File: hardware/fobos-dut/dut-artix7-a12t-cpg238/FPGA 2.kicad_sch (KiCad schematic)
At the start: 7 parts, among them U7 XC7A12T-CPG238

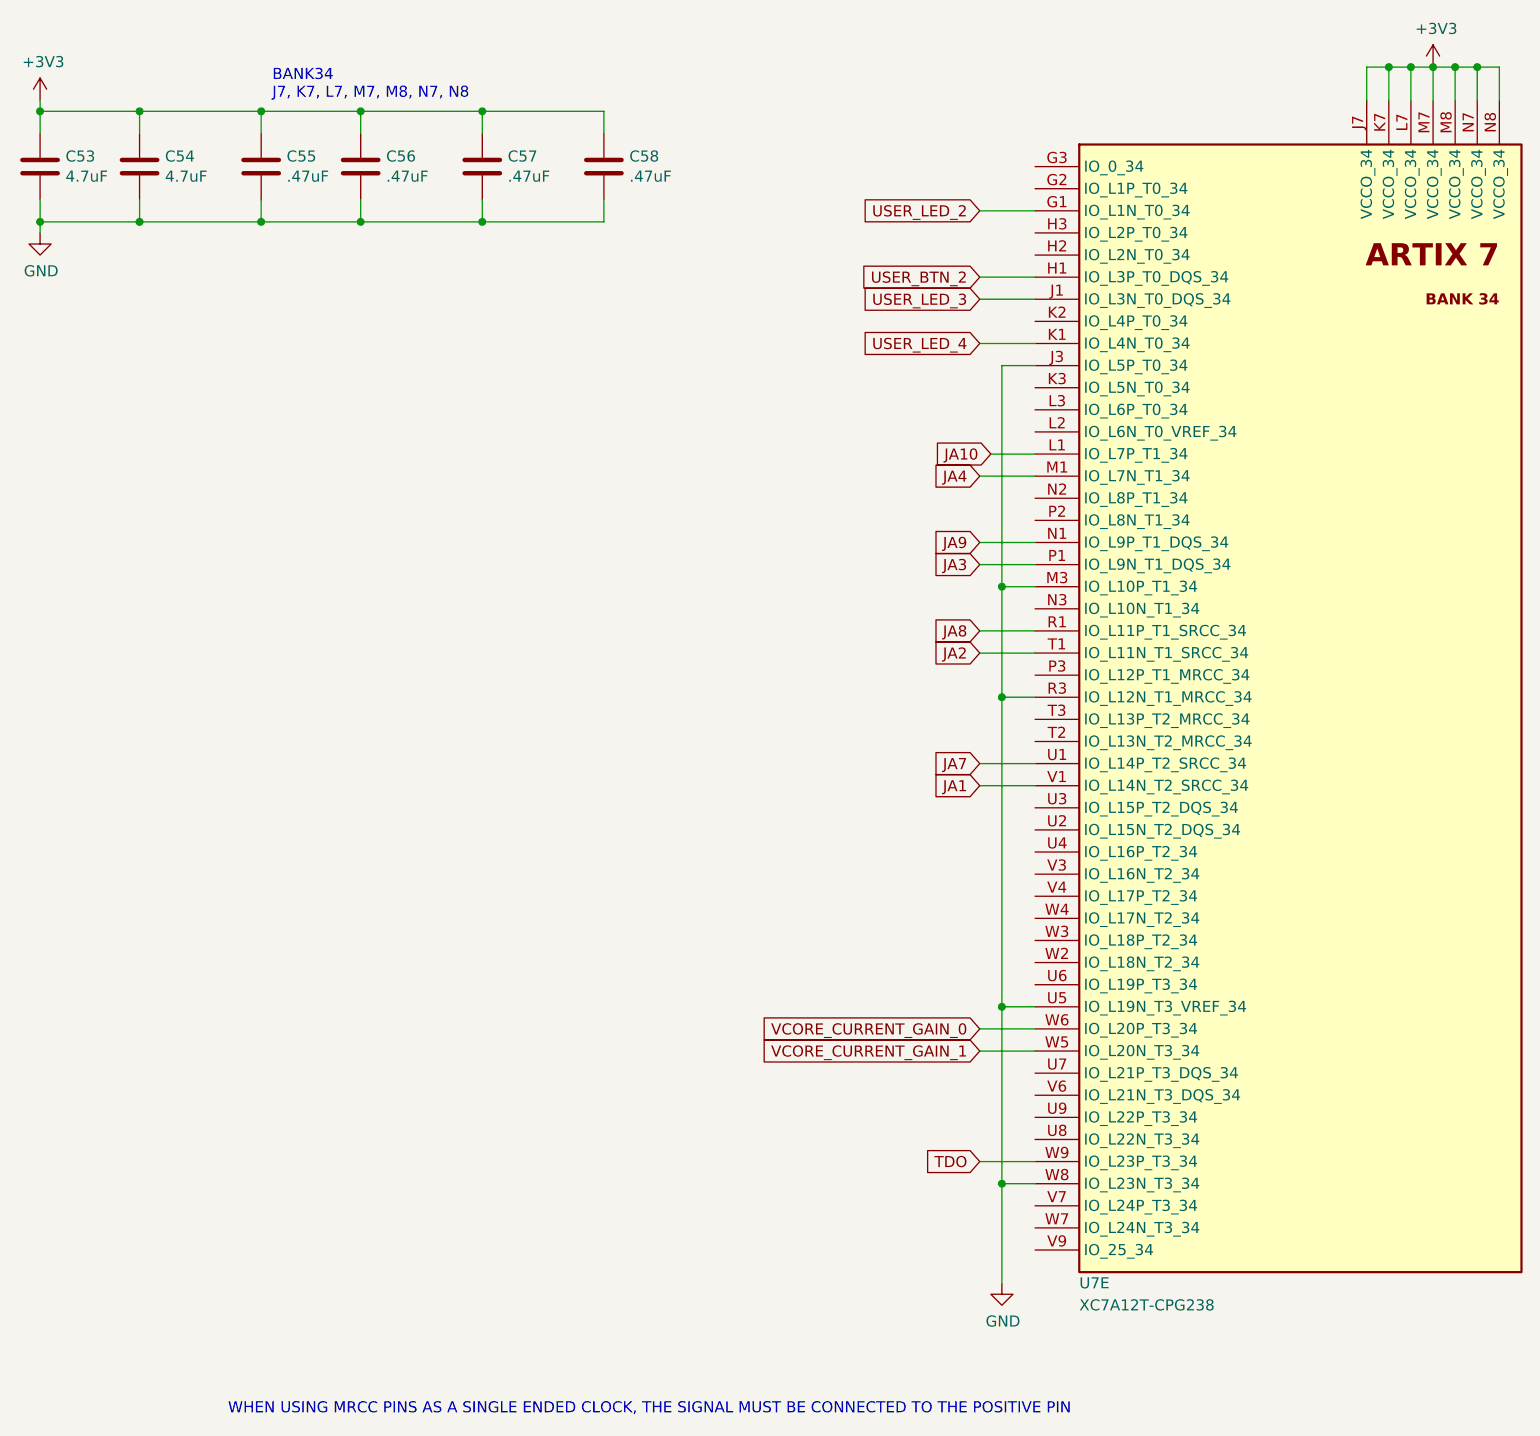
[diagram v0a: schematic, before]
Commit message: cleaned up FBDA7 rev1 added BOM, fixed bugs in schematic
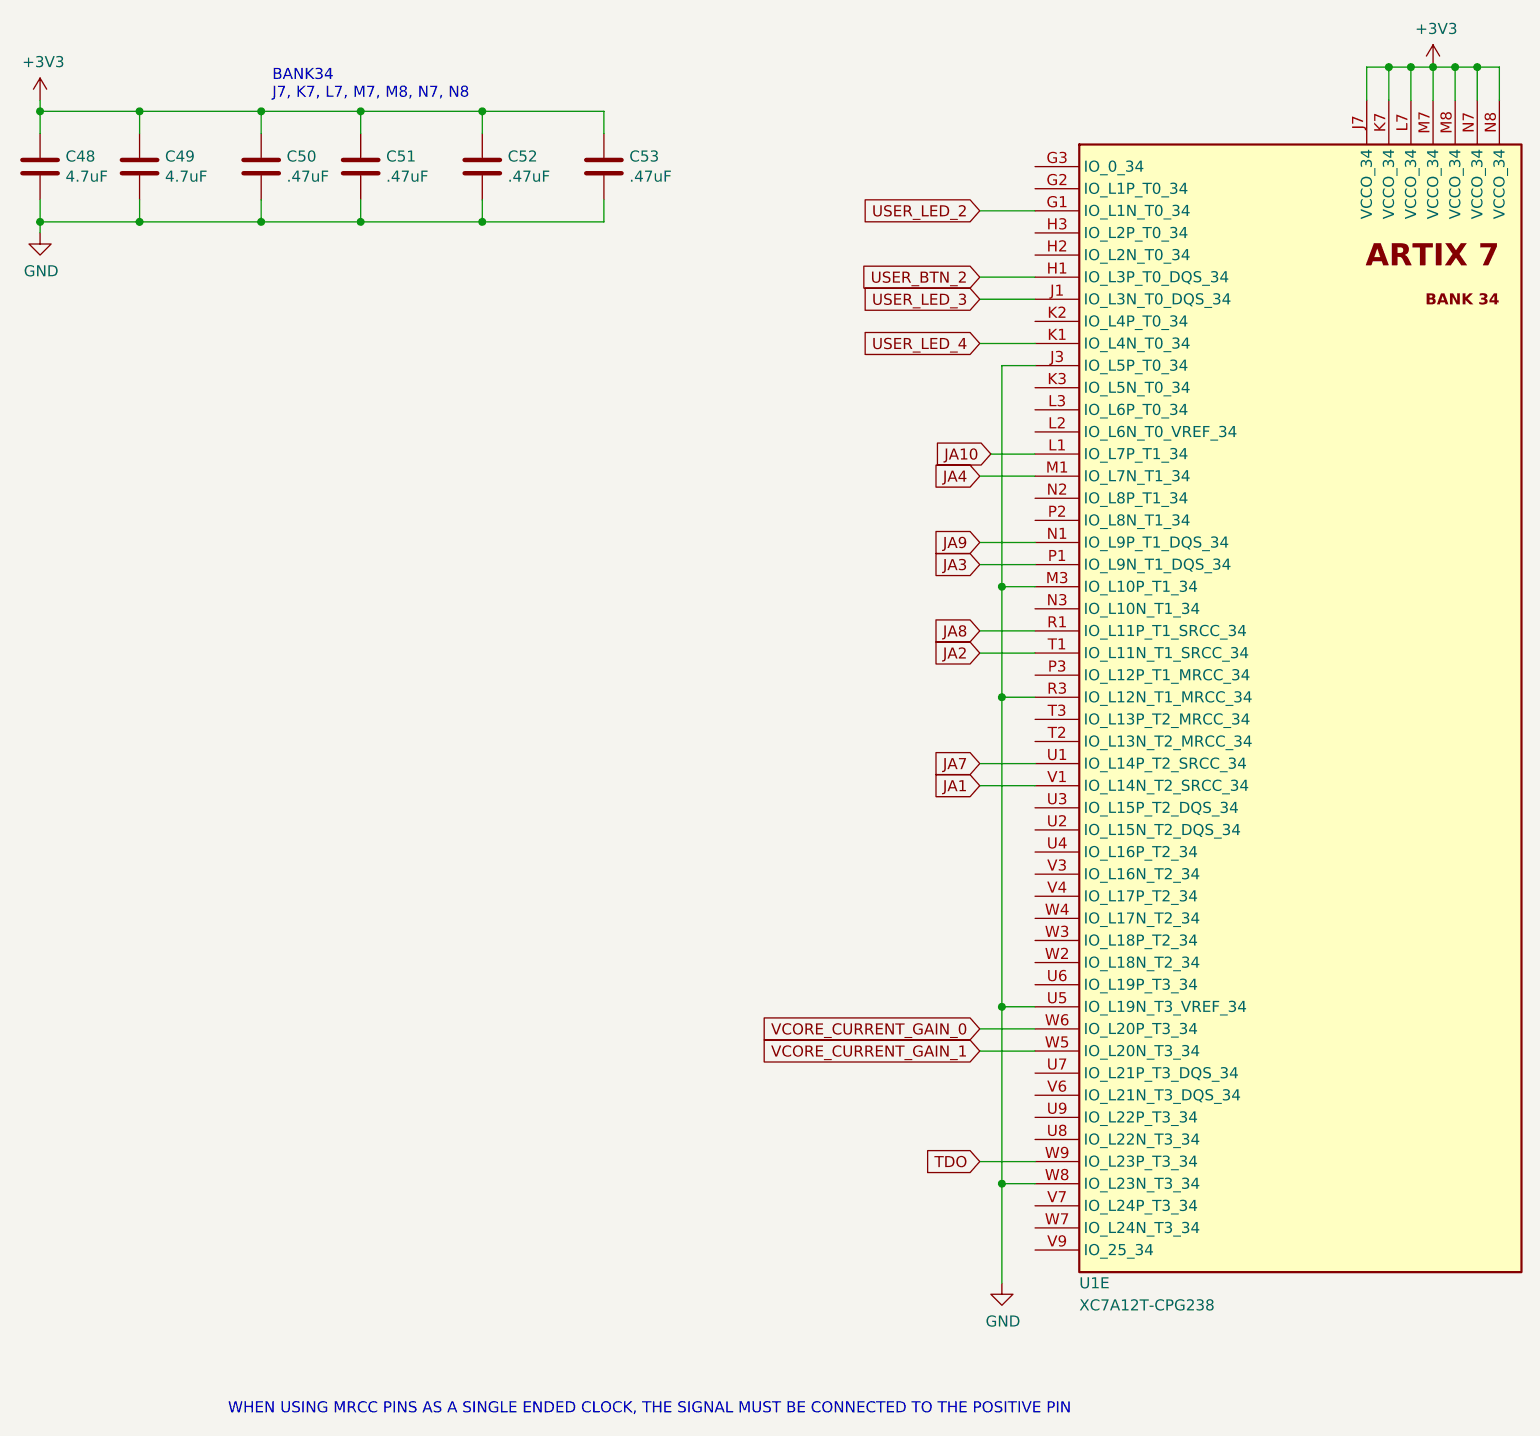
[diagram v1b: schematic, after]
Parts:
- renumbered C53 to C48, C54 to C49, C55 to C50, C56 to C51, C57 to C52, C58 to C53, U7 to U1
